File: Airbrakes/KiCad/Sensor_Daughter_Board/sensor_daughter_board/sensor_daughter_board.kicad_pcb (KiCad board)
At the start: 2 copper layers, 28 x 12 mm, 11 parts, among them U1 BMI088, U2 BMP581, U3 BMM350

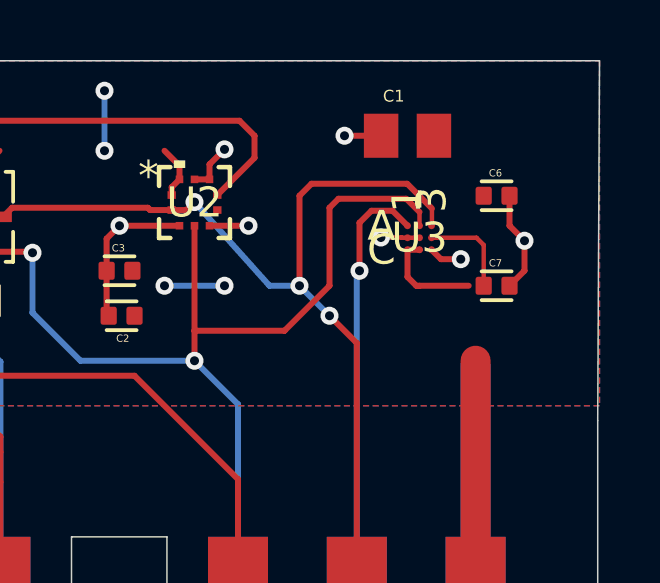
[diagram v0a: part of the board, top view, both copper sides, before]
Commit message: Make very minor change to via location
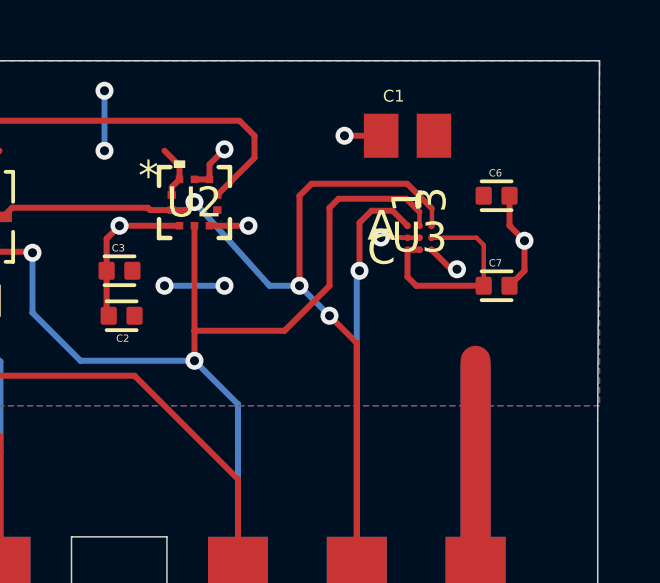
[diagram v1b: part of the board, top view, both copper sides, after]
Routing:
- net +3V3: track 26.7 -> 27.2 mm
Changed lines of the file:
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@@
-	)
-	(segment
-		(start 117.40005 43.3001)
-		(end 117.714015 43.614065)
-		(width 0.2)
-		(layer "F.Cu")
-		(net 3)
 	)
 	(segment
@@
 	)
 	(segment
-		(start 117.714015 43.614065)
-		(end 118.374578 43.614065)
-		(width 0.2)
-		(layer "F.Cu")
-		(net 3)
-	)
-	(segment
 		(start 99.7025 43.3675)
 		(end 99.7025 42.7975)
@@
 	)
 	(segment
+		(start 118.25 43.95)
+		(end 118.04995 43.95)
+		(width 0.2)
+		(layer "F.Cu")
+		(net 3)
+	)
+	(segment
 		(start 109.478833 40.975165)
 		(end 109.5 40.953998)
@@
 		(net 3)
 	)
+	(segment
+		(start 118.04995 43.95)
+		(end 117.40005 43.3001)
+		(width 0.2)
+		(layer "F.Cu")
+		(net 3)
+	)
 	(via
 		(at 101.2 42.2)
@@
 	)
 	(via
-		(at 118.374578 43.614065)
+		(at 118.25 43.95)
 		(size 0.6)
 		(drill 0.3)
@@
 	)
 	(segment
-		(start 116.59995 44.20715)
-		(end 116.59995 43.31435)
-		(width 0.2)
-		(layer "F.Cu")
-		(net 5)
-	)
-	(segment
 		(start 101.7025 44.853971)
 		(end 101.7025 43.3675)
+		(width 0.2)
+		(layer "F.Cu")
+		(net 5)
+	)
+	(segment
+		(start 119.14 44.5)
+		(end 116.8928 44.5)
 		(width 0.2)
 		(layer "F.Cu")
@@
 	)
 	(segment
-		(start 117 44.5)
-		(end 116.8928 44.5)
+		(start 116.59995 44.20715)
+		(end 116.59995 43.31435)
 		(width 0.2)
 		(layer "F.Cu")
@@
 	)
 	(segment
+		(start 109.000001 40.500001)
+		(end 108.5 40)
+		(width 0.2)
+		(layer "F.Cu")
+		(net 5)
+	)
+	(segment
+		(start 102.7025 40.2975)
+		(end 103 40)
+		(width 0.2)
+		(layer "F.Cu")
+		(net 5)
+	)
+	(segment
+		(start 118.90005 42.90005)
+		(end 119.14 43.14)
+		(width 0.15)
+		(layer "F.Cu")
+		(net 5)
+	)
+	(segment
 		(start 116.8928 44.5)
 		(end 116.59995 44.20715)
@@
 	)
 	(segment
-		(start 109.000001 40.500001)
-		(end 108.5 40)
-		(width 0.2)
-		(layer "F.Cu")
-		(net 5)
-	)
-	(segment
-		(start 102.7025 40.2975)
-		(end 103 40)
-		(width 0.2)
-		(layer "F.Cu")
-		(net 5)
-	)
-	(segment
-		(start 118.90005 42.90005)
-		(end 119.14 43.14)
-		(width 0.15)
-		(layer "F.Cu")
-		(net 5)
-	)
-	(segment
 		(start 108.739699 41.2143)
 		(end 109.000001 40.953998)
@@
 		(width 0.2)
 		(layer "F.Cu")
-		(net 5)
-	)
-	(segment
-		(start 118.64 44.5)
-		(end 117 44.5)
-		(width 0.2)
-		(layer "F.Cu")

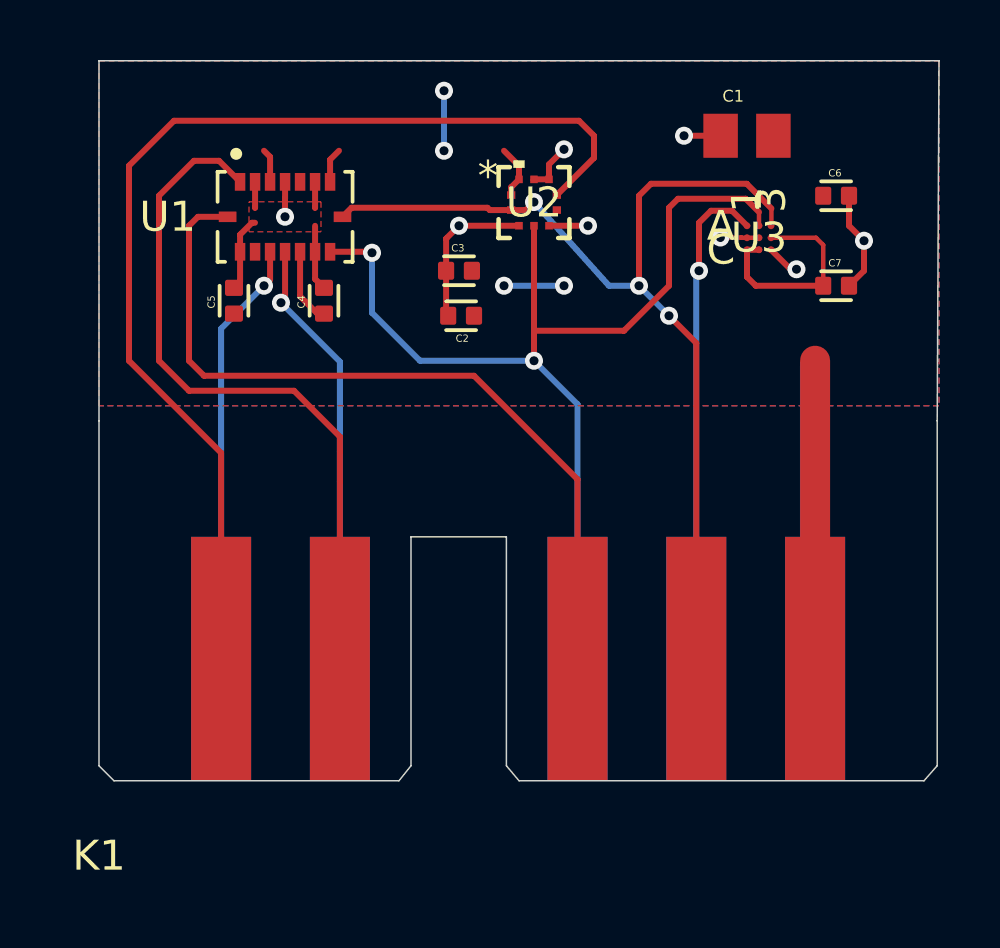
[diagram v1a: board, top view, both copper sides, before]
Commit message: make edge connected .2 mm smaller
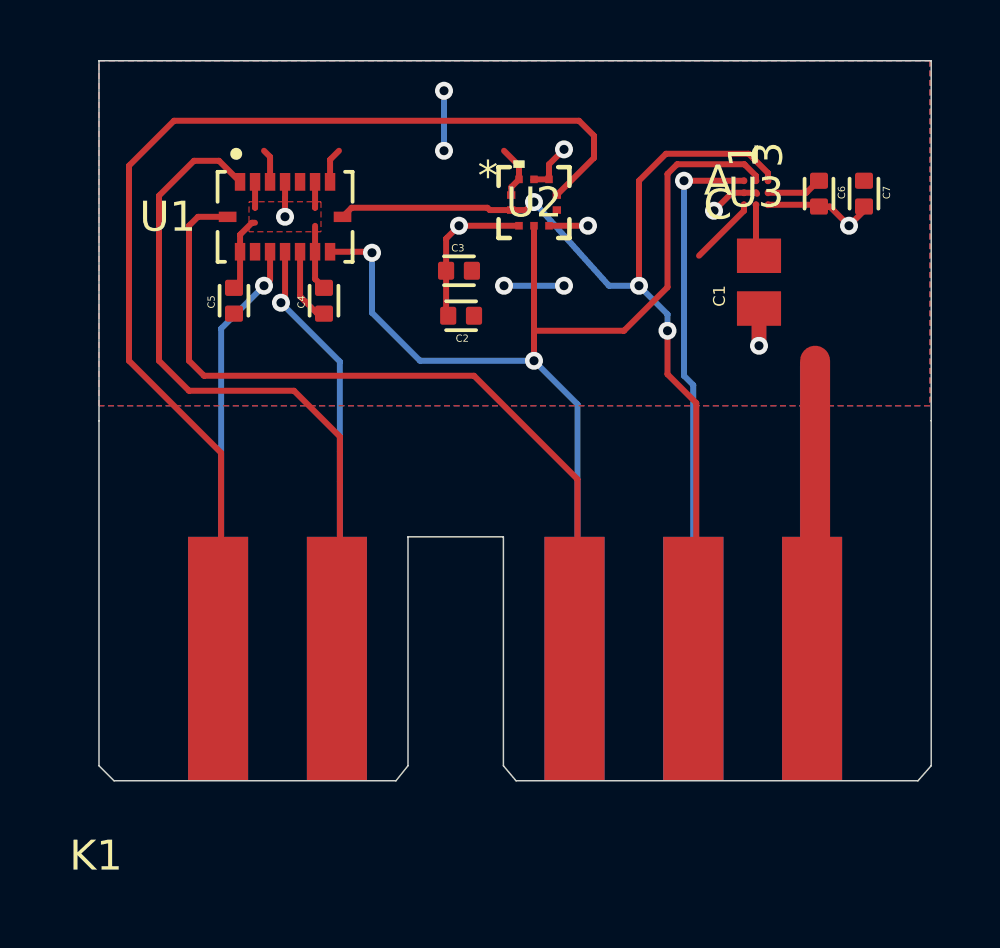
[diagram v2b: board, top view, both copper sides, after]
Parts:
- moved C1 4.90 mm to (117.0, 44.4), turned to 90 degrees
- moved C7 3.21 mm to (120.5, 41.4), turned to -90 degrees
- moved U3 1.50 mm to (116.9, 41.4)
- moved C6 0.57 mm to (119.0, 41.4), turned to -90 degrees
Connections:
- C1 pad 2: +3V3 -> /CRST
- U3 pad C2: +3V3 -> /CRST
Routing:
- net +3V3: track 27.2 -> 24.2 mm
- net MAG_INT: track 16.5 -> 18.6 mm
- net /CRST: track 0.00 -> 1.74 mm
- net SDA: track 36.0 -> 36.7 mm
- net GND: track 32.5 -> 32.2 mm, vias 8 -> 7
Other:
- board size 28 x 12 mm -> 27.7 x 12 mm

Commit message: silkscreens
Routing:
- net ACCEL_INT_2: track 23.0 -> 23.5 mm
